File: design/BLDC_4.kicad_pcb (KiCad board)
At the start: 4 copper layers, 38.5 x 65 mm, 127 parts, among them K1 SERVO, P1 HALL/Encoder, P101 CANBUS, P2 SWD, P3 PWR_COMM, P4 IN+, P5 IN-, P6 MOTOR1, P7 MOTOR2, P9 MOTOR3, Q1 IRFS7530, Q2 IRFS7530, Q3 IRFS7530, Q4 IRFS7530, Q5 IRFS7530, Q6 IRFS7530, U1 STM32F40X_LQFP64, U2 TC2117, U3 DRV8302, U401 SN65HVD232, X1 MINI-USB-SHIELD-32005-201, X2 8MHz 10ppm

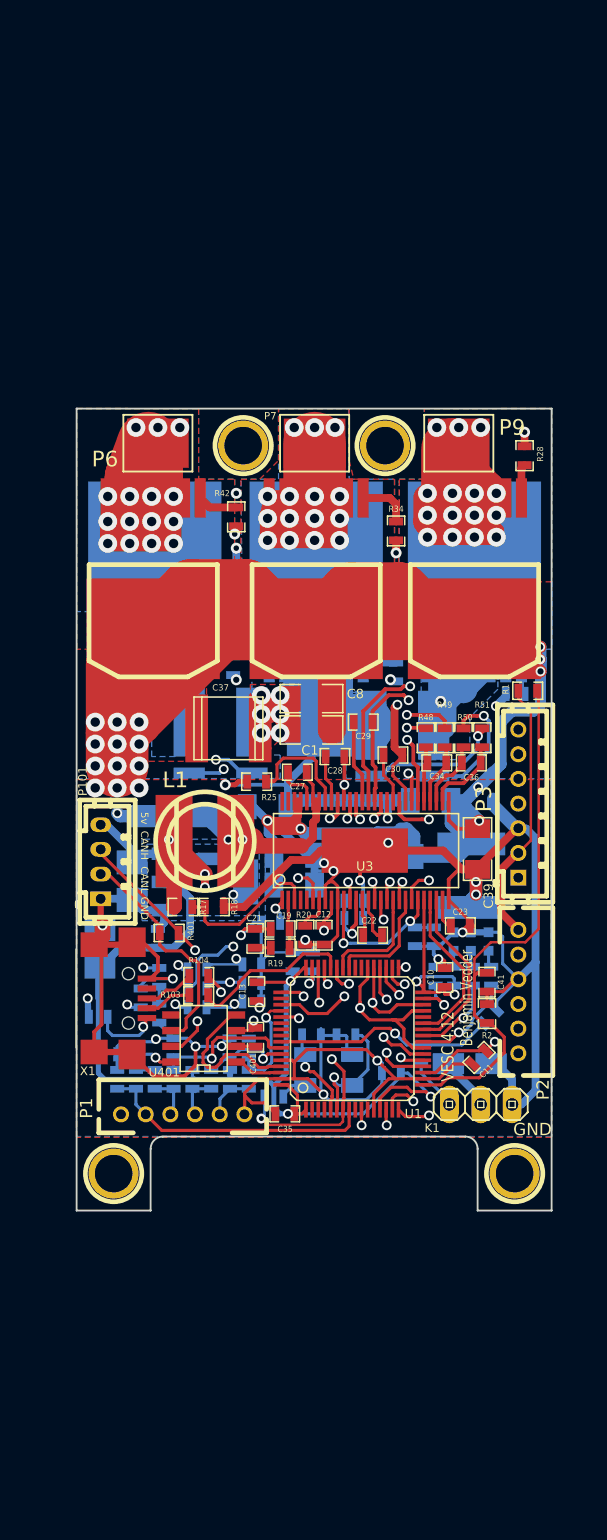
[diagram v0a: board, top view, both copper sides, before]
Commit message: changed to microusb
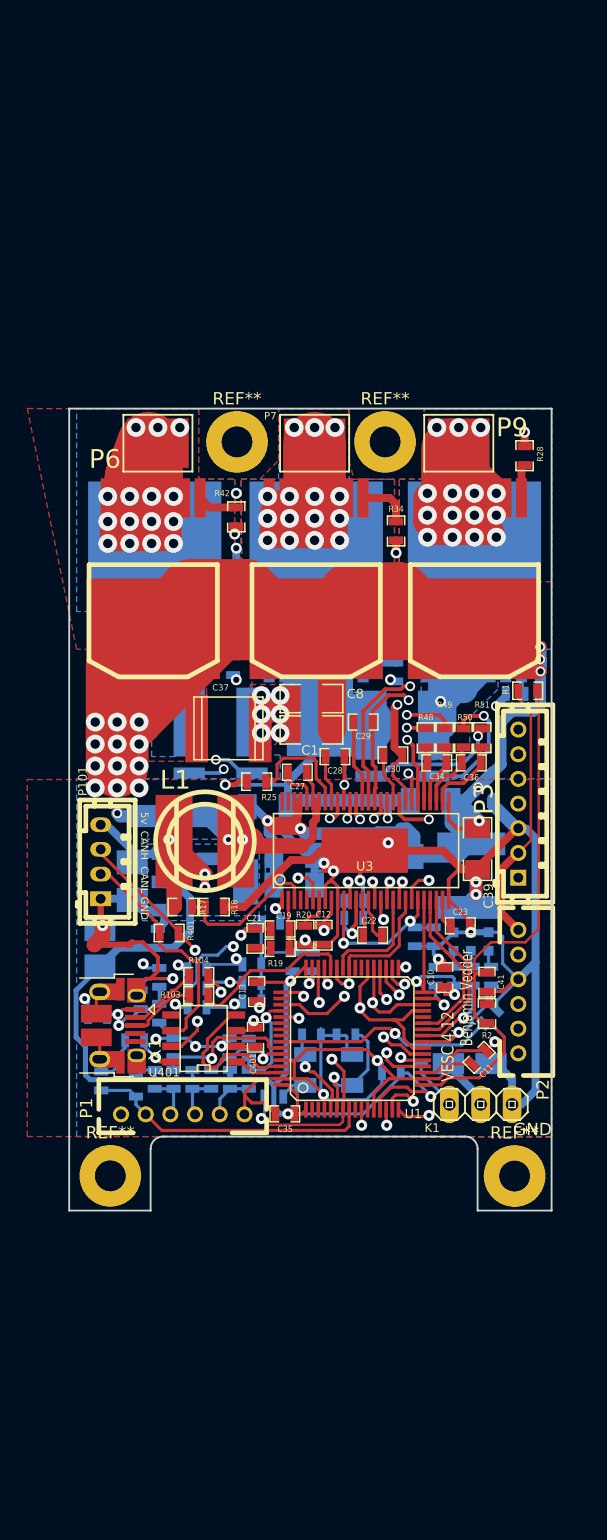
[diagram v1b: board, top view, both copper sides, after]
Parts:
- removed 1PIN (x2): P***, 1pin
- removed 1PIN (x2): P***, Connect:1pin
- removed G***: oshw_silkscreen-back_3mm, oshw_silkscreen-back_3mm
- added REF**: MountingHole_2.5mm_Pad, MountingHole:MountingHole_2.5mm_Pad, F.Cu at (81.2, 142.2)
- added REF**: MountingHole_2.5mm_Pad, MountingHole:MountingHole_2.5mm_Pad, F.Cu at (114.0, 142.2)
- added REF**: MountingHole_2.5mm_Pad, MountingHole:MountingHole_2.5mm_Pad, F.Cu at (103.5, 82.7)
- added REF**: MountingHole_2.5mm_Pad, MountingHole:MountingHole_2.5mm_Pad, F.Cu at (91.5, 82.7)
- R6: value 0R -> dnp
- X1: footprint CRF1:USB-UX60R-MB-5ST -> Connector_USB:USB_Micro-B_Amphenol_10103594-0001LF_Horizontal
- moved X1 2.54 mm to (81.5, 130.0)
- moved R402 1.31 mm to (83.2, 131.2)
- moved C4 1.29 mm to (80.5, 134.5)
- moved R7 0.63 mm to (83.3, 135.0)
- moved C2 0.14 mm to (83.7, 127.9)
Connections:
- net /Filters/TEMP_IN renamed /Filters/TEMP_MOTOR
- net /MCU/MISO_ADC_EXT2 renamed /MISO_RX_SCL
- net /MCU/RX_SCL_MOSI renamed /RX_SCL_MOSI
- net /MCU/SCK_ADC_EXT renamed /SCK_ADC_EXT
- net /MCU/TX_SDA_NSS renamed /TX_SDA
- P2 pad 6: Net-(P2-Pad6) -> unconnected-(P2-Pad6)
- R103 pad 2: Net-(R103-Pad2) -> Net-(X1-D+)
- R104 pad 2: Net-(R104-Pad2) -> Net-(X1-D-)
- U1 pad 11: Net-(U1-Pad11) -> unconnected-(U1-PC3(ADC123_IN13)-Pad11)
- U1 pad 2: Net-(U1-Pad2) -> unconnected-(U1-PC13_(RTC_AF1)-Pad2)
- U1 pad 28: Net-(U1-Pad28) -> unconnected-(U1-PB2-BOOT1-Pad28)
- U1 pad 3: Net-(U1-Pad3) -> unconnected-(U1-PC14-OSC32_IN-Pad3)
- U1 pad 39: Net-(U1-Pad39) -> unconnected-(U1-PC8-Pad39)
- U1 pad 4: Net-(U1-Pad4) -> unconnected-(U1-PC15-OSC32_OUT-Pad4)
- U1 pad 40: Net-(U1-Pad40) -> unconnected-(U1-PC9-Pad40)
- U1 pad 50: Net-(U1-Pad50) -> unconnected-(U1-PA15(JTDI)-Pad50)
- U1 pad 54: Net-(U1-Pad54) -> unconnected-(U1-PD2-Pad54)
- U1 pad 55: Net-(U1-Pad55) -> unconnected-(U1-PB3(JTDO/TRACESWO)-Pad55)
- U1 pad 56: Net-(U1-Pad56) -> unconnected-(U1-PB4(NJTRST)-Pad56)
- U1 pad 9: Net-(U1-Pad9) -> unconnected-(U1-PC1(ADC123_IN11)-Pad9)
- U3 pad 4: Net-(U3-Pad4) -> unconnected-(U3-PWRGD-Pad4)
- U3 pad 5: Net-(U3-Pad5) -> unconnected-(U3-OCTW-Pad5)
- U3 pad 55: Net-(U3-Pad55) -> unconnected-(U3-EN_BUCK-Pad55)
- U3 pad 56: Net-(U3-Pad56) -> unconnected-(U3-SS_TR-Pad56)
- U401 pad 5: Net-(U401-Pad5) -> unconnected-(U401-Vref-Pad5)
- X1 pad 2: Net-(R103-Pad2) -> Net-(X1-D-)
- X1 pad 3: Net-(R104-Pad2) -> Net-(X1-D+)
- X1 pad 4: Net-(X1-Pad4) -> unconnected-(X1-ID-Pad4)
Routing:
- net GND: track 398.8 -> 381.1 mm
- net Net-(X1-D-): track 0.00 -> 5.78 mm
- net Net-(X1-D+): track 0.00 -> 5.59 mm
- net Net-(R104-Pad2): track 4.28 -> 0.00 mm
- net Net-(R103-Pad2): track 3.97 -> 0.00 mm
- net Net-(X1-VBUS): track 5.50 -> 2.57 mm
- net VCC: track 185.2 -> 186.6 mm, vias 9 -> 8
- net /MCU/AN_IN: track 28.9 -> 30.1 mm
- net /Filters/TEMP_MOTOR: track 22.4 -> 23.3 mm
- added copper zone on In1.Cu, net /Mosfet driver/H1_VS
- added copper zone on In2.Cu, net /Mosfet driver/H1_VS
- added copper zone on In1.Cu, net /Mosfet driver/H2_VS
- added copper zone on In2.Cu, net /Mosfet driver/H2_VS
- added copper zone on In1.Cu, net /Mosfet driver/H3_VS
- added copper zone on In2.Cu, net /Mosfet driver/H3_VS
- added copper zone on In1.Cu, net GND
- added copper zone on In2.Cu, net GND
- removed copper zone on GND, net /Mosfet driver/H1_VS
- removed copper zone on GND2, net /Mosfet driver/H1_VS
- removed copper zone on GND, net /Mosfet driver/H2_VS
- removed copper zone on GND2, net /Mosfet driver/H2_VS
- removed copper zone on GND, net /Mosfet driver/H3_VS
- removed copper zone on GND2, net /Mosfet driver/H3_VS
- removed copper zone on GND, net GND
- removed copper zone on GND2, net GND
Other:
- board size 38.5 x 65 mm -> 39.1 x 65 mm
- net class Default removed

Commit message: work
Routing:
- net /MCU/DC_CAL: track 17.1 -> 18.7 mm
- net /MCU/AN_IN: track 30.1 -> 29.0 mm
- net GND: track 381.1 -> 380.5 mm
- net /Mosfet driver/H2_VS: track 145.0 -> 144.4 mm
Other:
- board text added: "BESC 4.12.1"
- board text removed: "Benjamin Vedder"
- board text removed: "VESC 4.12"

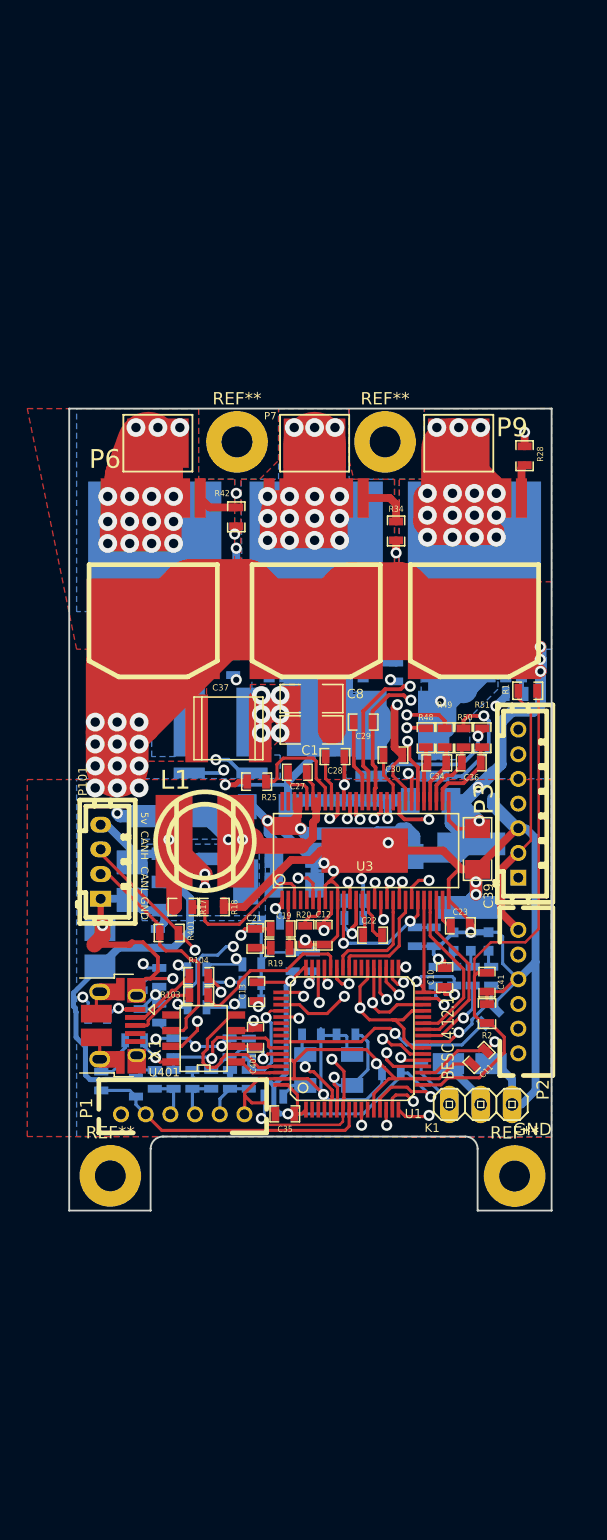
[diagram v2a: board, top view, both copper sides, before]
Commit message: first version ordered, working but USB wrong!
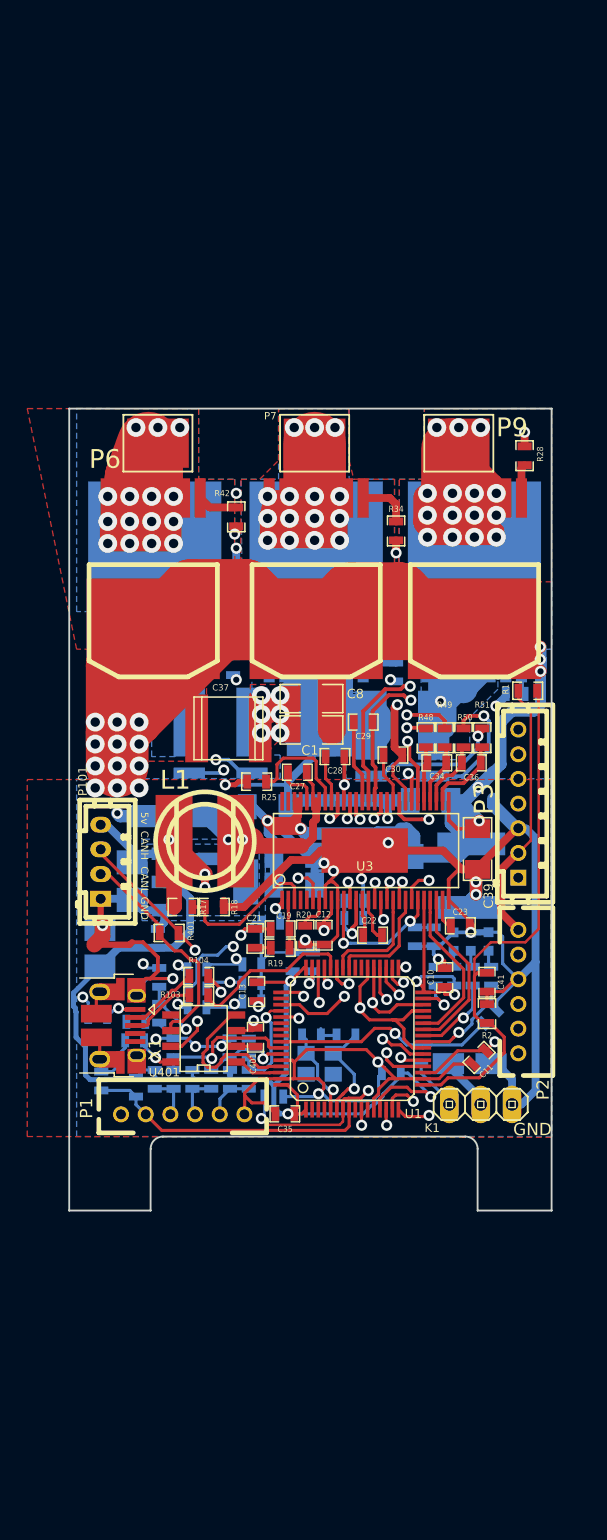
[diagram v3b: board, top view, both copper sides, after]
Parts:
- removed REF** (x4): MountingHole_2.5mm_Pad, MountingHole:MountingHole_2.5mm_Pad
- X2: footprint CRF1:Crystal_5x3mm -> Crystal:Crystal_SMD_3225-4Pin_3.2x2.5mm
- moved C2 1.84 mm to (83.3, 129.7), turned to 0 degrees
- moved X2 0.89 mm to (98.2, 133.1)
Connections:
- X2 pad 3: GND -> (no net)
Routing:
- net GND: track 380.5 -> 369.7 mm
- net Net-(U1-PH1-OSC_OUT): track 9.99 -> 8.53 mm
- net /MCU/AN_IN: track 29.0 -> 27.7 mm
- net +5V: track 115.9 -> 115.0 mm
- net /CAN bus transceiver/CANL: track 19.0 -> 18.4 mm
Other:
- board text removed: "vedder.se"

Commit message: extended board include input power caps and holes for wires
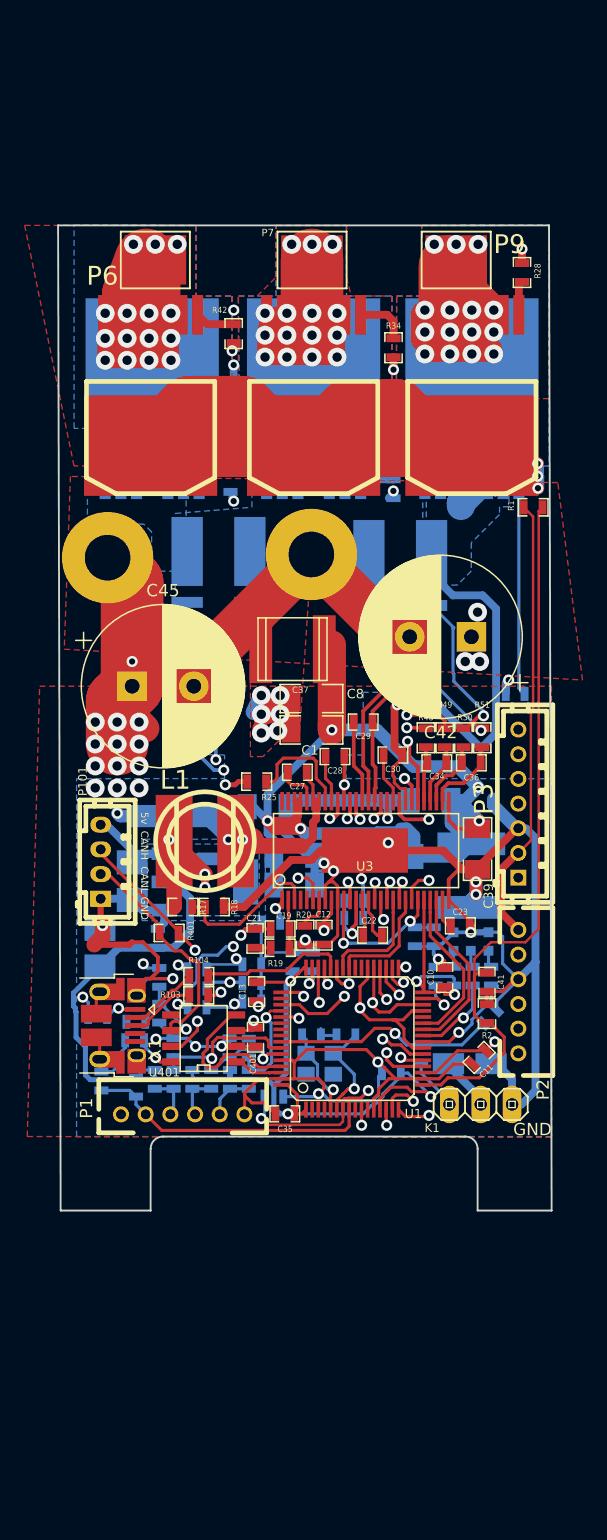
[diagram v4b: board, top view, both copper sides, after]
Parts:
- added C42: C_Polarized, Capacitor_THT:CP_Radial_D13.0mm_P5.00mm, F.Cu at (110.5, 98.5)
- added C45: C_Polarized, Capacitor_THT:CP_Radial_D13.0mm_P5.00mm, F.Cu at (83.0, 102.5)
- P4, P5: footprint CRF1:1PAD_4x5mm -> MountingHole:MountingHole_3.7mm_Pad
- R6: value dnp -> R0
- moved P4 16.0 mm to (81.0, 92.1)
- moved R1 14.9 mm to (115.5, 88.0)
- moved P6 14.8 mm to (84.9, 68.0)
- moved P7 14.8 mm to (97.6, 68.0)
- moved P9 14.8 mm to (109.3, 68.0)
- moved Q2 14.8 mm to (110.5, 81.0)
- moved Q4 14.8 mm to (97.7, 81.0)
- moved Q6 14.8 mm to (84.6, 81.0)
- moved R35 14.8 mm to (104.2, 86.5)
- moved R36 14.8 mm to (104.2, 84.0)
- moved Q1 14.8 mm to (110.5, 77.1)
- moved Q3 14.8 mm to (97.7, 77.1)
- moved Q5 14.8 mm to (84.5, 77.1)
- moved R28 14.8 mm to (114.6, 69.0)
- moved R30 14.8 mm to (104.2, 81.3)
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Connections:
- R103 pad 1: /MCU/USB_DM -> /MCU/USB_DP
- R104 pad 1: /MCU/USB_DP -> /MCU/USB_DM
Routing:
- net V_SUPPLY: track 290.0 -> 264.4 mm, vias 20 -> 22
- net /Mosfet driver/H1_LOW: track 48.5 -> 65.3 mm
- net /Mosfet driver/M_H3: track 40.9 -> 56.7 mm
- net /Mosfet driver/M_H2: track 24.4 -> 40.1 mm
- net /Mosfet driver/H1_VS: track 150.6 -> 166.2 mm
- net Net-(Q2-PadG): track 16.2 -> 31.4 mm
- net /Mosfet driver/M_H1: track 49.8 -> 64.9 mm
- net VCC: track 186.9 -> 201.7 mm
- net /Mosfet driver/H2_VS: track 144.4 -> 158.9 mm
- net /MCU/ADC_TEMP: track 44.0 -> 58.3 mm
- net /Mosfet driver/M_L2: track 19.3 -> 33.1 mm
- net GND: track 369.7 -> 357.3 mm, vias 27 -> 30
- net /Mosfet driver/M_L3: track 20.0 -> 31.2 mm
- net /Mosfet driver/SH1_A: track 24.0 -> 33.9 mm
- net /Mosfet driver/SH1_B: track 25.0 -> 34.8 mm
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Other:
- board size 39.1 x 65 mm -> 40 x 79.8 mm

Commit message: v 4.13 produced by jlcpcb
Some serious issues with usb connectors facing the caps. Working fine
otherwise
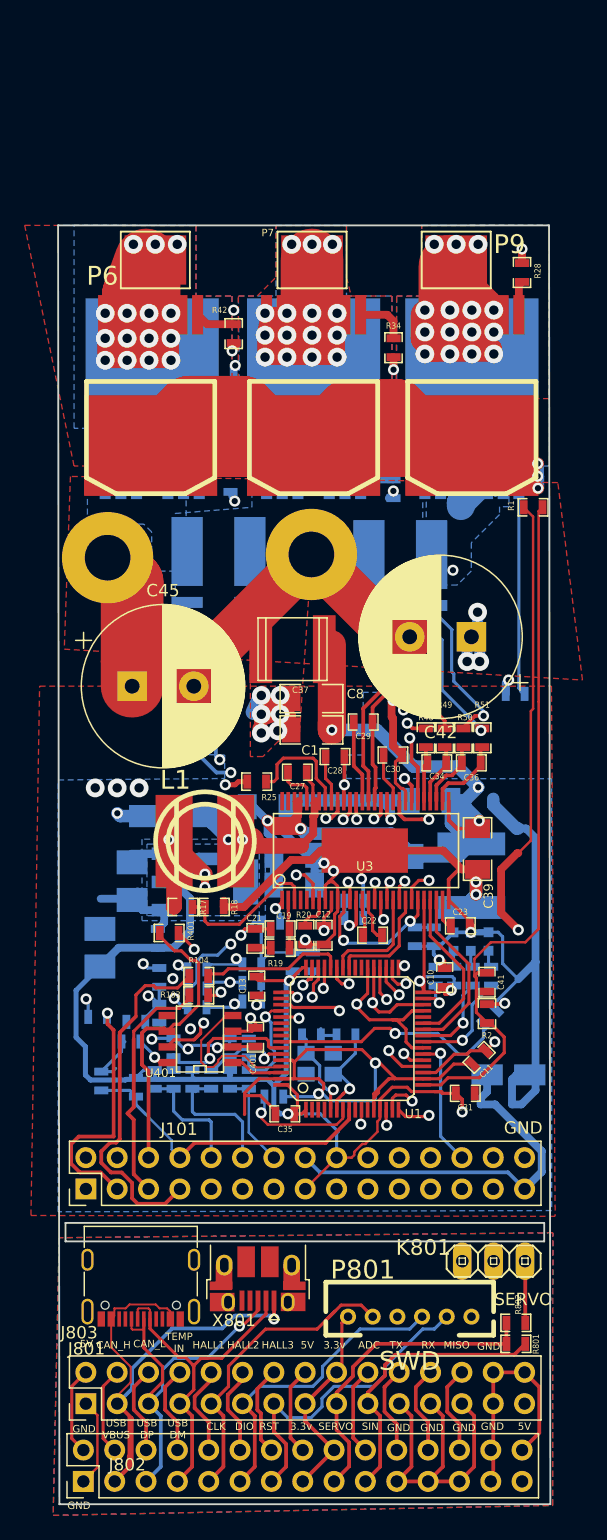
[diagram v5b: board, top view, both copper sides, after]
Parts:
- removed K1: SERVO, CRF1:pinhead-1X03
- removed P1: HALL/Encoder, CRF1:MICRO_JST_6
- removed P101: CANBUS, JST conn:b4b-ph-kl
- removed P2: SWD, CRF1:MICRO_JST_6
- removed P3: PWR_COMM, CRF1:b7b-ph-kl
- removed R5: 2k2, CRF1:SMD-0603_r
- removed X1: MINI-USB-SHIELD-32005-201, Connector_USB:USB_Micro-B_Amphenol_10103594-0001LF_Horizontal
- added J101: Conn_02x16_Odd_Even, Connector_PinHeader_2.54mm:PinHeader_2x15_P2.54mm_Vertical, F.Cu at (79.2, 143.2)
- added J801: Conn_02x16_Odd_Even, Connector_PinHeader_2.54mm:PinHeader_2x15_P2.54mm_Vertical, F.Cu at (79.2, 160.7)
- added J802: Conn_02x16_Odd_Even, Connector_PinHeader_2.54mm:PinHeader_2x15_P2.54mm_Vertical, F.Cu at (79.0, 166.9)
- added J803: USB_C_Receptacle_USB2.0_16P, Connector_USB:USB_C_Receptacle_G-Switch_GT-USB-7010ASV, F.Cu at (83.7, 150.1)
- added K801: SERVO, CRF1:pinhead-1X03, F.Cu at (112.3, 149.1)
- added P801: SWD, CRF1:MICRO_JST_6, F.Cu at (105.5, 153.6)
- added R801: 2k2, CRF1:SMD-0603_r, F.Cu at (114.1, 155.8)
- added R802: 100R, CRF1:SMD-0603_r, F.Cu at (114.1, 154.1)
- added X801: MINI-USB-SHIELD-32005-201, Connector_USB:USB_Micro-B_Amphenol_10103594-0001LF_Horizontal, F.Cu at (93.2, 150.5)
- C31: moved to F.Cu
- C39: value 10u,50V -> 10u,63V
- moved C31 6.21 mm to (110.0, 135.5), turned to 180 degrees
- moved D5 3.26 mm to (113.5, 134.0)
- moved C13 0.45 mm to (93.1, 126.8)
- moved R402 0.32 mm to (82.9, 131.3)
- moved U401 0.30 mm to (88.5, 131.1)
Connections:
- net /CAN bus transceiver/CANH renamed /CAN_H
- net /CAN bus transceiver/CANL renamed /CAN_L
- net /Filters/HALL1_IN renamed /HALL1
- net /Filters/HALL2_IN renamed /HALL2
- net /Filters/HALL3_IN renamed /HALL3
- net /Filters/TEMP_MOTOR renamed /TEMP_IN
- net /MCU/SERVO renamed /SERVO_SIGNAL
- R103 pad 2: Net-(X1-D+) -> /USB_DP
- R104 pad 2: Net-(X1-D-) -> /USB_DM
- R6 pad 1: Net-(X1-VBUS) -> /USB_VBUS
- X2 pad 2: Net-(U1-PH1-OSC_OUT) -> GND
- X2 pad 3: (no net) -> Net-(U1-PH1-OSC_OUT)
- X2 pad 4: (no net) -> GND
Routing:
- net /connboard/GND: track 0.00 -> 52.7 mm
- net /connboard/USB_VBUS: track 0.00 -> 48.7 mm, vias 0 -> 1
- net GND: track 357.3 -> 320.5 mm, vias 30 -> 29
- net V_SUPPLY: track 264.4 -> 228.1 mm, vias 22 -> 12
- net +5V: track 115.0 -> 82.7 mm
- net /connboard/USB_DP: track 0.00 -> 31.5 mm, vias 0 -> 1
- net /connboard/USB_DM: track 0.00 -> 31.2 mm
- net /USB_DM: track 0.00 -> 29.1 mm
- net VCC: track 201.7 -> 230.5 mm, vias 8 -> 10
- net /connboard/SWCLK: track 0.00 -> 26.7 mm
- net /connboard/NRST: track 0.00 -> 25.9 mm
- net /connboard/SERVO_SIGNAL: track 0.00 -> 25.7 mm
- net /MISO_RX_SCL: track 36.0 -> 10.6 mm
- net /connboard/SWDIO: track 0.00 -> 25.2 mm
- net /connboard/SERVO_INPUT: track 0.00 -> 23.0 mm
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- added copper zone on In1.Cu, net +5V
- added copper zone on In2.Cu, net /connboard/5V
- added copper zone on B.Cu, net /connboard/GND
- added copper zone on F.Cu, net /connboard/GND
- added copper zone on In1.Cu, net /connboard/GND
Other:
- board size 40 x 79.8 mm -> 39.9 x 103.6 mm
- board text added: "5V"
- board text added: "BESC ${version}"
- board text added: "CAN_H"
- board text added: "CAN_L"
- board text added: "HALL1"
- board text added: "HALL2"
- board text added: "HALL3"
- board text added: "SERVO"
- board text added: "SIN"
- board text added: "TEMP IN"
- board text added: "USB DM"
- board text added: "USB DP"
- board text added: "USB VBUS"
- board text removed: "3.3V"
- board text removed: "5v"
- board text removed: "ADC2"
- board text removed: "BESC 4.12.1"
- board text removed: "CANH"
- board text removed: "CANL"
- board text removed: "H1"
- board text removed: "H2"
- board text removed: "H3"
- board text removed: "MOSI"
- board text removed: "NSS"
- board text removed: "SCK"
- board text removed: "SCL"
- board text removed: "SDA"
- board text removed: "TEMP"
